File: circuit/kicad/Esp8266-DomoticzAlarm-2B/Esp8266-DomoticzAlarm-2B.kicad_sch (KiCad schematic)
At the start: 30 parts, among them J1 Barrel_Jack_Switch, J2 Sensor, J3 CAM_DI, Q1 BC817, Q2 BC817, U1 CH32V003JxMx, U2 ESP-12E, U4 MIC5219-3.3YM5

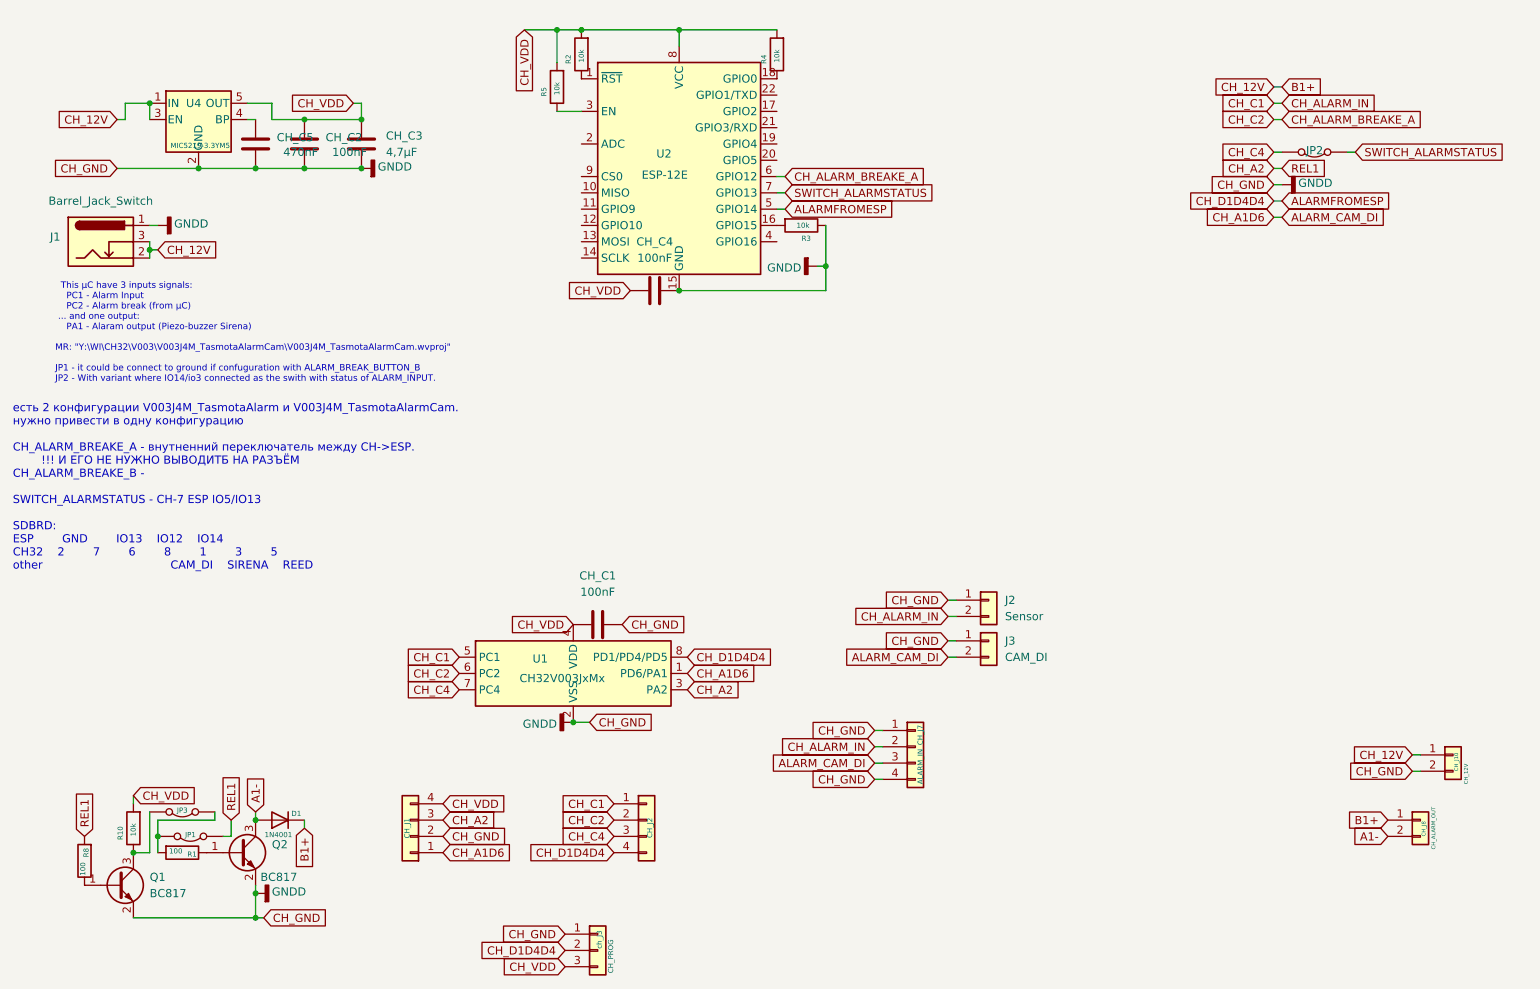
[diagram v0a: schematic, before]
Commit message: circuit: power over HT7333. PDF. READ.md
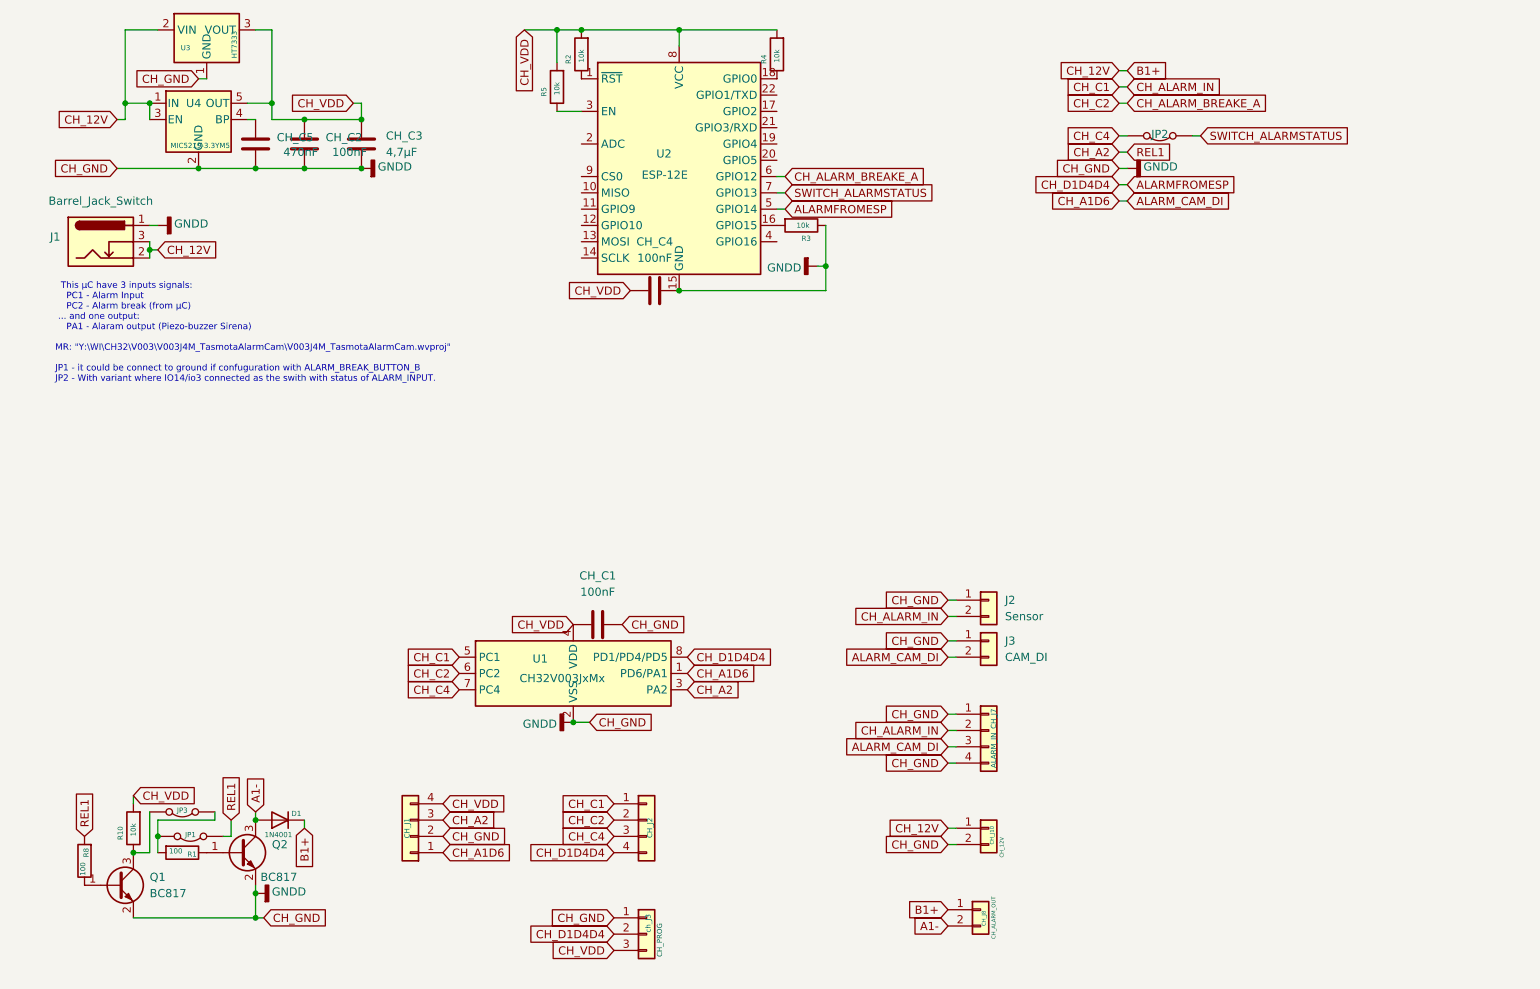
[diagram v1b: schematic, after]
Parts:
- added U3: HT7333, Package_TO_SOT_SMD:SOT-89-3, symbol Regulator_Linear:HT75xx-1-SOT89
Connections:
- net B1+: now also U3.2 (VIN)
- net CH_VDD: now also U3.3 (VOUT)
- net GNDD: now also U3.1 (GND)
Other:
- note removed: "есть 2 конфигурации V003J4M_TasmotaAlarm и V003J4M_TasmotaAlarmCam. нужно привести в одну конфигурацию CH_ALARM_BREAKE_A - внутненний переключатель между CH->ESP. !!! И ЕГО НЕ НУЖНО ВЫВОДИТБ НА РАЗЪЁМ CH_ALARM_BREAKE_B - SWITCH_ALARMSTATUS - CH-7 ESP IO5/IO13 SDBRD: ESP GND IO13 IO12 IO14 CH32 2 7 6 8 1 3 5 other CAM_DI SIRENA REED"
- moved on the sheet: CH_J10, CH_J7, CH_J8, JP2, ch_J3

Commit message: little changes in PCB
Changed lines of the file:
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@@
 		(on_board yes)
 		(dnp no)
-		(fields_autoplaced yes)
 		(property "Reference" "CH_C3"
-			(at 72.39 34.2899 0)
+			(at 69.088 32.766 0)
 			(effects
 				(font
@@
 		)
 		(property "Value" "4,7µF"
-			(at 72.39 36.8299 0)
+			(at 71.12 36.83 0)
 			(effects
 				(font
@@
 		(dnp no)
 		(property "Reference" "CH_C5"
-			(at 55.372 34.544 0)
+			(at 49.022 41.148 0)
 			(effects
 				(font
@@
 		)
 		(property "Value" "470nF"
-			(at 56.388 36.83 0)
+			(at 49.022 43.434 0)
 			(effects
 				(font
@@
 		(dnp no)
 		(property "Reference" "CH_C2"
-			(at 62.992 34.544 0)
+			(at 60.452 33.274 0)
 			(effects
 				(font
@@
 		)
 		(property "Value" "100nF"
-			(at 64.008 36.83 0)
-			(effects
-				(font
+			(at 60.198 38.1 0)
+			(effects
+				(font

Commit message: changes 20260416
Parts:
- added D2: 1N5819WS, Diode_SMD:D_SOD-323_HandSoldering, symbol Diode:1N5819WS
- CH_C2, CH_C4: footprint Capacitor_SMD:C_0805_2012Metric -> Capacitor_SMD:C_1206_3216Metric
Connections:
- net B1+: now also D2.1 (K); no longer J1.2, J1.3
- net GNDD: now also J1.2, J1.3; no longer J1.1
- new net: D2.2 (A), J1.1
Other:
- company: (none) -> (C) SVDdevelop
- title: (none) -> TasmotaCamAlarmSirena
- moved on the sheet: CH_C1
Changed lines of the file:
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@@
 	(generator_version "9.0")
 	(paper "A4")
+	(title_block
+		(title "TasmotaCamAlarmSirena")
+		(date "2026-04-04")
+		(rev "1.2")
+		(company "(C) SVDdevelop")
+	)
 	(text "  This µC have 3 inputs signals:\n    PC1 - Alarm Input\n    PC2 - Alarm break (from µC)\n ... and one output: \n    PA1 - Alaram output (Piezo-buzzer Sirena)\n\nMR: \"Y:\\WI\\CH32\\V003\\V003J4M_TasmotaAlarmCam\\V003J4M_TasmotaAlarmCam.wvproj\"\n\nJP1 - it could be connect to ground if confuguration with ALARM_BREAK_BUTTON_B\nJP2 - With variant where IO14/io3 connected as the swith with status of ALARM_INPUT.\n"
 		(exclude_from_sim no)
@@
 	)
 	(junction
+		(at 35.56 52.07)
+		(diameter 0)
+		(color 0 0 0 0)
+	)
+	(junction
 		(at 140.97 54.61)
 		(diameter 0)
@@
 	)
 	(junction
-		(at 68.58 39.37)
+		(at 101.6 110.49)
 		(diameter 0)
 		(color 0 0 0 0)
 	)
 	(junction
-		(at 99.06 17.78)
+		(at 68.58 39.37)
 		(diameter 0)
 		(color 0 0 0 0)
 	)
 	(junction
-		(at 118.11 58.42)
+		(at 99.06 17.78)
 		(diameter 0)
 		(color 0 0 0 0)
 	)
 	(junction
-		(at 35.56 52.07)
+		(at 118.11 58.42)
 		(diameter 0)
 		(color 0 0 0 0)
@@
 	(wire
 		(pts
+			(xy 35.56 52.07) (xy 35.56 53.34)
+		)
+		(stroke
+			(width 0)
+			(type default)
+		)
+	)
+	(wire
+		(pts
 			(xy 160.02 132.08) (xy 161.29 132.08)
 		)
@@
 	(wire
 		(pts
-			(xy 35.56 48.26) (xy 36.83 48.26)
+			(xy 31.75 31.75) (xy 31.75 29.21)
 		)
 		(stroke
@@
 	(wire
 		(pts
-			(xy 31.75 31.75) (xy 31.75 29.21)
+			(xy 48.26 143.51) (xy 48.26 140.97)
 		)
 		(stroke
@@
 	(wire
 		(pts
-			(xy 48.26 143.51) (xy 48.26 140.97)
+			(xy 186.69 44.45) (xy 187.96 44.45)
 		)
 		(stroke
@@
 	(wire
 		(pts
-			(xy 186.69 44.45) (xy 187.96 44.45)
+			(xy 52.07 152.4) (xy 52.07 151.13)
 		)
 		(stroke
@@
 	(wire
 		(pts
-			(xy 52.07 152.4) (xy 52.07 151.13)
+			(xy 186.69 39.37) (xy 187.96 39.37)
 		)
 		(stroke
@@
 	(wire
 		(pts
-			(xy 186.69 39.37) (xy 187.96 39.37)
+			(xy 100.33 110.49) (xy 101.6 110.49)
 		)
 		(stroke
@@
 	(wire
 		(pts
+			(xy 35.56 48.26) (xy 36.83 48.26)
+		)
+		(stroke
+			(width 0)
+			(type default)
+		)
+	)
+	(wire
+		(pts
 			(xy 43.18 39.37) (xy 52.07 39.37)
 		)
@@
 	(wire
 		(pts
-			(xy 35.56 52.07) (xy 35.56 53.34)
+			(xy 44.45 48.26) (xy 45.72 48.26)
+		)
+		(stroke
+			(width 0)
+			(type default)
+		)
+	)
+	(wire
+		(pts
+			(xy 111.76 110.49) (xy 110.49 110.49)
 		)
 		(stroke
@@
 	(wire
 		(pts
+			(xy 35.56 52.07) (xy 36.83 52.07)
+		)
+		(stroke
+			(width 0)
+			(type default)
+		)
+	)
+	(wire
+		(pts
 			(xy 36.83 140.97) (xy 36.83 143.51)
 		)
@@
 	(wire
 		(pts
-			(xy 35.56 52.07) (xy 36.83 52.07)
+			(xy 102.87 110.49) (xy 101.6 110.49)
 		)
 		(stroke
@@
 	(wire
 		(pts
+			(xy 100.33 125.73) (xy 101.6 125.73)
+		)
+		(stroke
+			(width 0)
+			(type default)
+		)
+	)
+	(wire
+		(pts
 			(xy 45.72 139.7) (xy 45.72 140.97)
 		)
@@
 	(global_label "CH_12V"
 		(shape input)
-		(at 36.83 52.07 0)
+		(at 45.72 48.26 0)
 		(fields_autoplaced yes)
 		(effects
@@
 		)
 		(property "Intersheetrefs" "${INTERSHEET_REFS}"
-			(at 46.8909 52.07 0)
+			(at 55.7809 48.26 0)
 			(effects
 				(font
@@
 	(global_label "CH_GND"
 		(shape input)
-		(at 109.22 110.49 0)
+		(at 111.76 110.49 0)
 		(fields_autoplaced yes)
 		(effects
@@
 		)
 		(property "Intersheetrefs" "${INTERSHEET_REFS}"
-			(at 119.6438 110.49 0)
+			(at 122.1838 110.49 0)
 			(effects
 				(font
@@
 	(global_label "CH_VDD"
 		(shape input)
-		(at 101.6 110.49 180)
+		(at 100.33 110.49 180)
 		(fields_autoplaced yes)
 		(effects
@@
 		)
 		(property "Intersheetrefs" "${INTERSHEET_REFS}"
-			(at 91.4181 110.49 0)
+			(at 90.1481 110.49 0)
 			(effects
 				(font
@@
 		(on_board yes)
 		(dnp no)
-		(fields_autoplaced yes)
 		(property "Reference" "CH_C4"
-			(at 114.3 50.8 90)
+			(at 114.808 61.976 90)
 			(effects
 				(font
@@
 		)
 		(property "Value" "100nF"
-			(at 114.3 53.34 90)
+			(at 114.808 63.754 90)
 			(effects
 				(font
@@
 			)
 		)
-		(property "Footprint" "Capacitor_SMD:C_0805_2012Metric"
+		(property "Footprint" "Capacitor_SMD:C_1206_3216Metric"
 			(at 118.11 57.4548 0)
 			(effects
@@
 	(symbol
 		(lib_id "Device:C")
-		(at 105.41 110.49 90)
+		(at 106.68 110.49 90)
 		(unit 1)
 		(exclude_from_sim no)
@@
 		(fields_autoplaced yes)
 		(property "Reference" "CH_C1"
-			(at 105.41 102.87 90)
+			(at 106.68 102.87 90)
 			(effects
 				(font
@@
 		)
 		(property "Value" "100nF"
-			(at 105.41 105.41 90)
+			(at 106.68 105.41 90)
 			(effects
 				(font
@@
 		)
 		(property "Footprint" "Capacitor_SMD:C_0805_2012Metric"
-			(at 109.22 109.5248 0)
+			(at 110.49 109.5248 0)
 			(effects
 				(font
@@
 		)
 		(property "Datasheet" "~"
-			(at 105.41 110.49 0)
+			(at 106.68 110.49 0)
 			(effects
 				(font
@@
 		)
 		(property "Description" "Unpolarized capacitor"
-			(at 105.41 110.49 0)
+			(at 106.68 110.49 0)
 			(effects
 				(font
@@
 			)
 		)
-		(property "Footprint" "Capacitor_SMD:C_0805_2012Metric"
+		(property "Footprint" "Capacitor_SMD:C_1206_3216Metric"
 			(at 58.7248 31.75 0)
 			(effects
@@
 	(symbol
 		(lib_id "power:GNDD")
-		(at 101.6 125.73 270)
+		(at 100.33 125.73 270)
 		(unit 1)
 		(exclude_from_sim no)
@@
 		(dnp no)
 		(property "Reference" "#PWR04"
-			(at 95.25 125.73 0)
+			(at 93.98 125.73 0)
 			(effects
 				(font
@@
 		)
 		(property "Value" "GNDD"
-			(at 99.06 125.984 90)
+			(at 97.79 125.984 90)
 			(effects
 				(font
@@
 		)
 		(property "Footprint" ""
-			(at 101.6 125.73 0)
+			(at 100.33 125.73 0)
 			(effects
 				(font
@@
 		)
 		(property "Datasheet" ""
-			(at 101.6 125.73 0)
+			(at 100.33 125.73 0)
 			(effects
 				(font
@@
 		)
 		(property "Description" "Power symbol creates a global label with name \"GNDD\" , digital ground"
-			(at 101.6 125.73 0)
+			(at 100.33 125.73 0)
 			(effects
 				(font
@@
 	(symbol
 		(lib_id "power:GNDD")
-		(at 36.83 48.26 90)
+		(at 36.83 52.07 90)
 		(unit 1)
 		(exclude_from_sim no)
@@
 		(dnp no)
 		(property "Reference" "#PWR06"
-			(at 43.18 48.26 0)
+			(at 43.18 52.07 0)
 			(effects
 				(font
@@
 		)
 		(property "Value" "GNDD"
-			(at 39.37 48.006 90)
+			(at 39.37 51.816 90)
 			(effects
 				(font
@@
 		)
 		(property "Footprint" ""
-			(at 36.83 48.26 0)
+			(at 36.83 52.07 0)
 			(effects
 				(font
@@
 		)
 		(property "Datasheet" ""
-			(at 36.83 48.26 0)
+			(at 36.83 52.07 0)
 			(effects
 				(font
@@
 		)
 		(property "Description" "Power symbol creates a global label with name \"GNDD\" , digital ground"
-			(at 36.83 48.26 0)
+			(at 36.83 52.07 0)
 			(effects
 				(font
@@
 					(unit 1)
 				)
+			)
+		)
+	)
+	(symbol
+		(lib_id "Diode:1N5819WS")
+		(at 40.64 48.26 180)
+		(unit 1)
+		(exclude_from_sim no)
+		(in_bom yes)
+		(on_board yes)
+		(dnp no)
+		(fields_autoplaced yes)
+		(property "Reference" "D2"
+			(at 40.9575 41.91 0)
+			(effects
+				(font
+					(size 1.27 1.27)
+				)
+				(hide yes)
+			)
+		)
+		(property "Value" "1N5819WS"
+			(at 40.9575 44.45 0)
+			(effects
+				(font
+					(size 1.27 1.27)
+				)
+				(hide yes)
+			)
+		)
+		(property "Footprint" "Diode_SMD:D_SOD-323_HandSoldering"
+			(at 40.64 43.815 0)
+			(effects
+				(font
+					(size 1.27 1.27)
+				)
+				(hide yes)
+			)
+		)
+		(property "Datasheet" "https://datasheet.lcsc.com/lcsc/2204281430_Guangdong-Hottech-1N5819WS_C191023.pdf"
+			(at 40.64 48.26 0)
+			(effects
+				(font
+					(size 1.27 1.27)
+				)
+				(hide yes)
+			)
+		)
+		(property "Description" "40V 600mV@1A 1A SOD-323 Schottky Barrier Diodes, SOD-323"
+			(at 40.64 48.26 0)
+			(effects
+				(font
+					(size 1.27 1.27)
+				)
+				(hide yes)
+			)
+		)
+		(pin "2"
+		)
+		(pin "1"
+		)
+		(instances
+			(project ""
+				(path "/e1345bf2-2850-4d6e-a7ea-3c40f0f448c6"
+					(reference "D2")
+					(unit 1)
+				)
